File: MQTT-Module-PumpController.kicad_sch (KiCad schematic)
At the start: 0 parts

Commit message: Updated schematic and board with adjustments, updated board.
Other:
- sheet Controller ports: added {UPDI}; removed {UDPI}
- sheet Headers ports: added {UPDI}; removed {UDPI}
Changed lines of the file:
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@@
+	(bus
+		(pts
+			(xy 179.07 104.14) (xy 179.07 80.01)
+		)
+		(stroke
+			(width 0)
+			(type default)
+		)
+	)
 	(bus
 		(pts
@@
 	(bus
 		(pts
-			(xy 179.07 104.14) (xy 179.07 80.01)
+			(xy 179.07 80.01) (xy 182.88 80.01)
 		)
 		(stroke
@@
 		(pts
 			(xy 229.87 104.14) (xy 229.87 73.66)
-		)
-		(stroke
-			(width 0)
-			(type default)
-		)
-	)
-	(bus
-		(pts
-			(xy 179.07 80.01) (xy 182.88 80.01)
 		)
 		(stroke
@@
 			)
 		)
-		(pin "{UDPI}" input
+		(pin "{UPDI}" bidirectional
 			(at 179.07 104.14 90)
 			(effects
@@
 			)
 		)
-		(pin "{UDPI}" bidirectional
+		(pin "{UPDI}" bidirectional
 			(at 182.88 80.01 180)
 			(effects

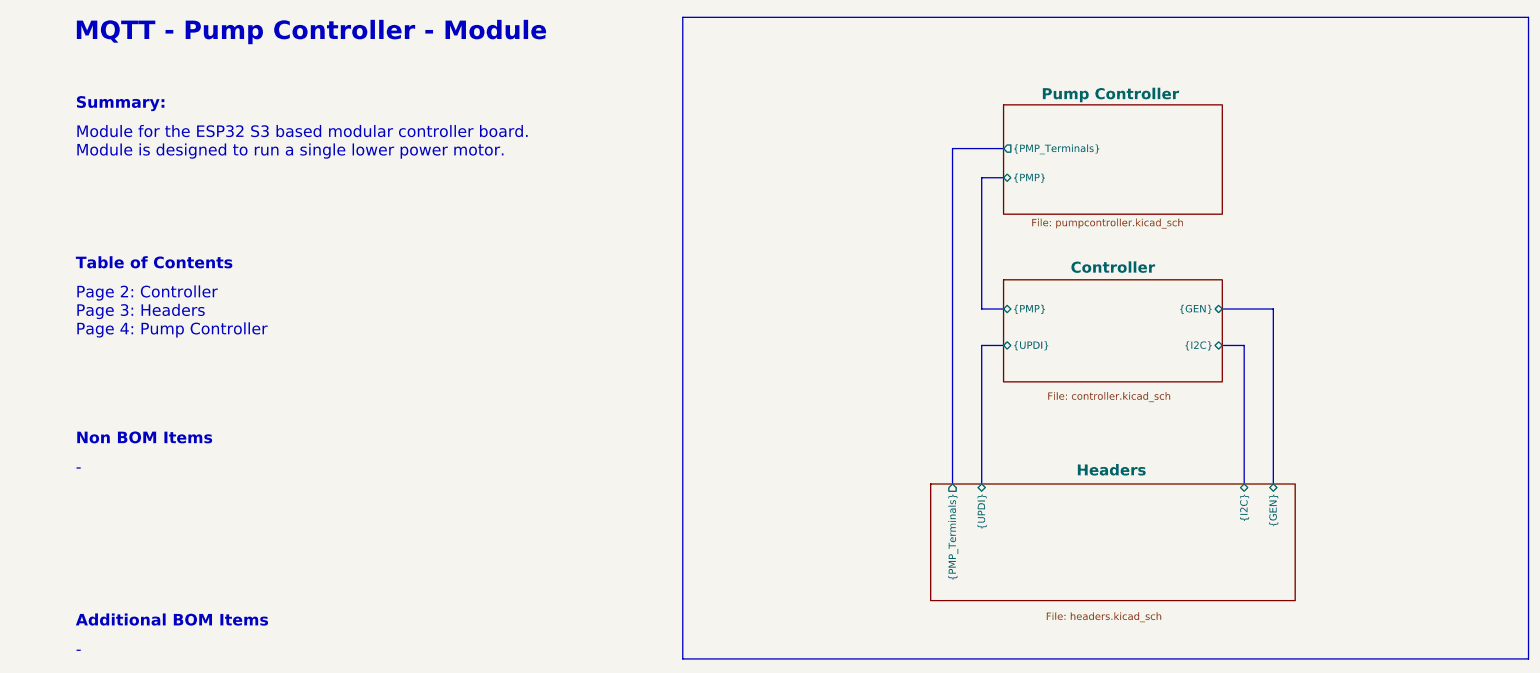
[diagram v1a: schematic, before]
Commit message: Updated schematic, redesigned and included pump pressure switch. Regenerated all outputs.
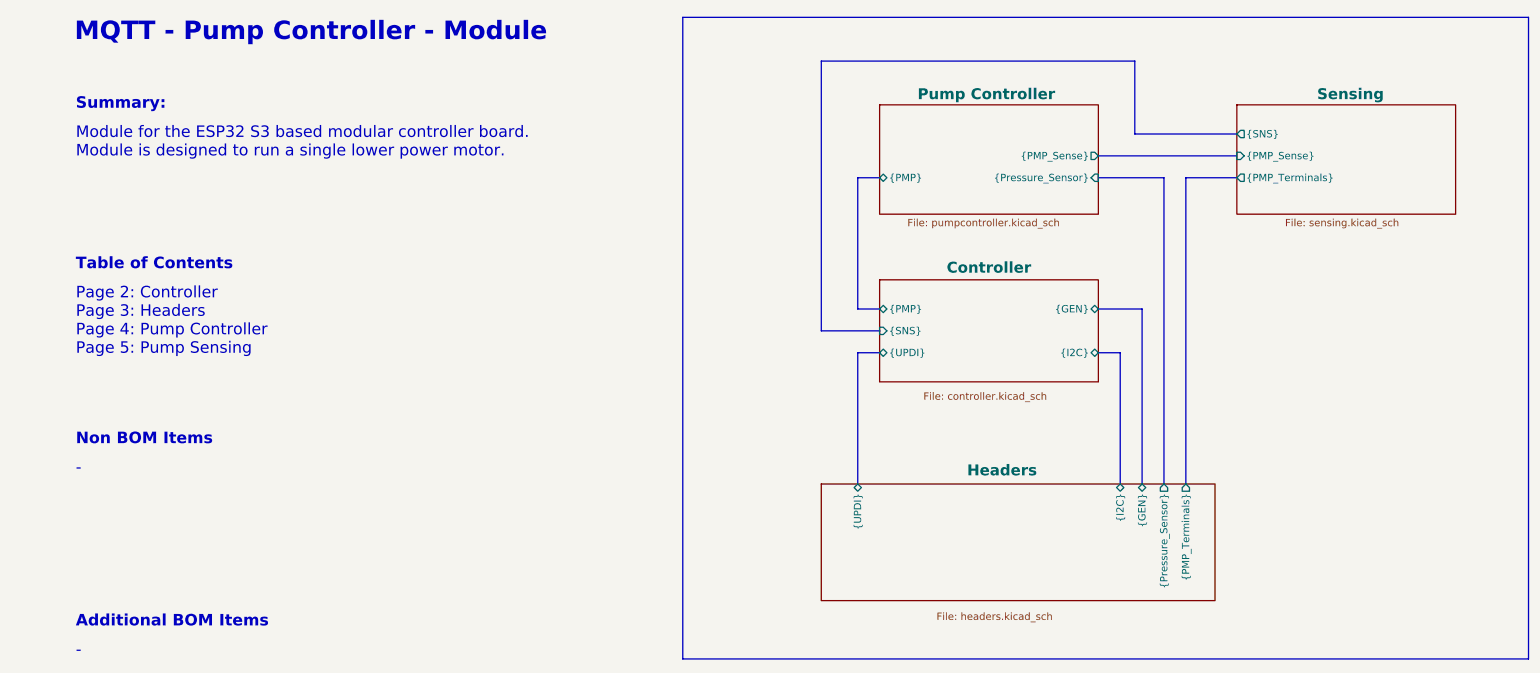
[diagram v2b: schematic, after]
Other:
- added sheet Sensing (sensing.kicad_sch)
- sheet Controller ports: added {SNS}; removed none
- sheet Headers ports: added {Pressure_Sensor}; removed none
- sheet Pump Controller ports: added {PMP_Sense}, {Pressure_Sensor}; removed {PMP_Terminals}
